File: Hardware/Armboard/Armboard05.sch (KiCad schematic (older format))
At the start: 0 parts

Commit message: Added, Solenoid actuation, laser control, and encoders
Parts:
- added Conn?: Molex_SL_02, symbol MRDT_Connectors:Molex_SL_02
- added D?: LED, symbol Device:LED
- added Q?: Q_NMOS_GSD, symbol Device:Q_NMOS_GSD
- added R?: 1.5k, symbol Device:R
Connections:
- new net: Conn?.2, D?.1 (K), Q?.3 (D)
- new net: D?.2 (A), R?.2
- new net +12V: Conn?.1, R?.1
- new net GND: Q?.2 (S)
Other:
- note added: "Orange"
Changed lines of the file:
@@
 Comment4 ""
 $EndDescr
+$Comp
+L MRDT_Connectors:Molex_SL_02 Conn?
+U 1 1 5F79C943
+P 5850 3250
+F 0 "Conn?" H 5978 3408 60  0000 L CNN
+F 1 "Molex_SL_02" H 5978 3302 60  0000 L CNN
+F 2 "" H 5850 3150 60  0001 C CNN
+F 3 "" H 5850 3150 60  0001 C CNN
+	1    5850 3250
+	1    0    0    -1
+$EndComp
+$Comp
+L power:+12V #PWR?
+U 1 1 5F79C949
+P 5300 2850
+AR Path="/5F73890D/5F79C949" Ref="#PWR?"  Part="1"
+AR Path="/5F738767/5F79C949" Ref="#PWR?"  Part="1"
+F 0 "#PWR?" H 5300 2700 50  0001 C CNN
+F 1 "+12V" H 5315 3023 50  0000 C CNN
+F 2 "" H 5300 2850 50  0001 C CNN
+F 3 "" H 5300 2850 50  0001 C CNN
+	1    5300 2850
+	1    0    0    -1
+$EndComp
+$Comp
+L power:GND #PWR?
+U 1 1 5F79C94F
+P 5300 4850
+F 0 "#PWR?" H 5300 4600 50  0001 C CNN
+F 1 "GND" H 5305 4677 50  0000 C CNN
+F 2 "" H 5300 4850 50  0001 C CNN
+F 3 "" H 5300 4850 50  0001 C CNN
+	1    5300 4850
+	1    0    0    -1
+$EndComp
+$Comp
+L Device:Q_NMOS_GSD Q?
+U 1 1 5F79C957
+P 5200 4400
+F 0 "Q?" H 5404 4446 50  0000 L CNN
+F 1 "Q_NMOS_GSD" H 5404 4355 50  0000 L CNN
+F 2 "" H 5400 4500 50  0001 C CNN
+F 3 "~" H 5200 4400 50  0001 C CNN
+	1    5200 4400
+	1    0    0    -1
+$EndComp
+Wire Wire Line
+	5300 4850 5300 4600
+$Comp
+L Device:R R?
+U 1 1 5F79C95E
+P 5300 3450
+AR Path="/5F73890D/5F79C95E" Ref="R?"  Part="1"
+AR Path="/5F738767/5F79C95E" Ref="R?"  Part="1"
+F 0 "R?" H 5370 3496 50  0000 L CNN
+F 1 "1.5k" H 5370 3405 50  0000 L CNN
+F 2 "" V 5230 3450 50  0001 C CNN
+F 3 "~" H 5300 3450 50  0001 C CNN
+	1    5300 3450
+	1    0    0    -1
+$EndComp
+$Comp
+L Device:LED D?
+U 1 1 5F79C964
+P 5300 3900
+F 0 "D?" V 5339 3782 50  0000 R CNN
+F 1 "LED" V 5248 3782 50  0000 R CNN
+F 2 "" H 5300 3900 50  0001 C CNN
+F 3 "~" H 5300 3900 50  0001 C CNN
+	1    5300 3900
+	0    -1   -1   0
+$EndComp
+Wire Wire Line
+	5300 3750 5300 3600
+Wire Wire Line
+	5300 4200 5300 4150
+Wire Wire Line
+	5650 3200 5600 3200
+Wire Wire Line
+	5650 3100 5300 3100
+Wire Wire Line
+	5300 3100 5300 3300
+Wire Wire Line
+	5600 3200 5600 4150
+Wire Wire Line
+	5600 4150 5300 4150
+Connection ~ 5300 4150
+Wire Wire Line
+	5300 4150 5300 4050
+Wire Wire Line
+	5300 3100 5300 2850
+Connection ~ 5300 3100
+Text Notes 4950 3950 0    50   ~ 0
+Orange
 $EndSCHEMATC

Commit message: H-Bridge completed
Completed the H-Bridge Hierarchal Sheet
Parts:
- Conn?: symbol MRDT_Connectors:Molex_SL_02 -> Armboard-rescue:Molex_SL_02-MRDT_Connectors
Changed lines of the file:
@@
 $EndDescr
 $Comp
-L MRDT_Connectors:Molex_SL_02 Conn?
+L Armboard-rescue:Molex_SL_02-MRDT_Connectors Conn?
 U 1 1 5F79C943
 P 5850 3250

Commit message: Added serial pins, limit switches, titles, and indicators
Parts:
- added D?: LED, symbol Device:LED
- added R?: 500, symbol Device:R
- Conn?: symbol Armboard-rescue:Molex_SL_02-MRDT_Connectors -> Armboard-rescue:Molex_SL_02-MRDT_Connectors-Armboard-rescue
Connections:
- net GND: now also D?.1 (K)
- net Solenoid_Actuation: now reaches Q?.1 (G)
- net Solenoid_Actuation: now also R?.1
- new net: D?.2 (A), R?.2
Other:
- note added: "Solenoid Actuation"
- note added: "Yellow"
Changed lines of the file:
@@
 $EndDescr
 $Comp
-L Armboard-rescue:Molex_SL_02-MRDT_Connectors Conn?
+L Armboard-rescue:Molex_SL_02-MRDT_Connectors-Armboard-rescue Conn?
 U 1 1 5F79C943
 P 5850 3250
@@
 Text Notes 4950 3950 0    50   ~ 0
 Orange
+Text GLabel 4500 4400 0    50   Input ~ 0
+Solenoid_Actuation
+$Comp
+L Device:R R?
+U 1 1 5F8410BE
+P 4750 4700
+AR Path="/5F73890D/5F8410BE" Ref="R?"  Part="1"
+AR Path="/5F738767/5F8410BE" Ref="R?"  Part="1"
+F 0 "R?" H 4820 4746 50  0000 L CNN
+F 1 "500" H 4820 4655 50  0000 L CNN
+F 2 "" V 4680 4700 50  0001 C CNN
+F 3 "~" H 4750 4700 50  0001 C CNN
+	1    4750 4700
+	1    0    0    -1
+$EndComp
+$Comp
+L Device:LED D?
+U 1 1 5F841F2B
+P 4750 5100
+F 0 "D?" V 4789 4982 50  0000 R CNN
+F 1 "LED" V 4698 4982 50  0000 R CNN
+F 2 "" H 4750 5100 50  0001 C CNN
+F 3 "~" H 4750 5100 50  0001 C CNN
+	1    4750 5100
+	0    -1   -1   0
+$EndComp
+Text Notes 4400 5150 0    50   ~ 0
+Yellow
+$Comp
+L power:GND #PWR?
+U 1 1 5F842098
+P 4750 5350
+F 0 "#PWR?" H 4750 5100 50  0001 C CNN
+F 1 "GND" H 4755 5177 50  0000 C CNN
+F 2 "" H 4750 5350 50  0001 C CNN
+F 3 "" H 4750 5350 50  0001 C CNN
+	1    4750 5350
+	1    0    0    -1
+$EndComp
+Wire Wire Line
+	4500 4400 4750 4400
+Wire Wire Line
+	4750 4550 4750 4400
+Connection ~ 4750 4400
+Wire Wire Line
+	4750 4400 5000 4400
+Wire Wire Line
+	4750 4950 4750 4850
+Wire Wire Line
+	4750 5350 4750 5250
+Text Notes 6500 7150 0    157  ~ 31
+Solenoid Actuation
 $EndSCHEMATC

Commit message: Tiva Updates
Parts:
- added SW?: SW_Push, symbol Switch:SW_Push
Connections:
- net +12V: now also SW?.2; no longer R?.1
- new net: R?.1, SW?.1
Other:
- moved on the sheet: Conn?
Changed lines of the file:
@@
 L Armboard-rescue:Molex_SL_02-MRDT_Connectors-Armboard-rescue Conn?
 U 1 1 5F79C943
-P 5850 3250
-F 0 "Conn?" H 5978 3408 60  0000 L CNN
-F 1 "Molex_SL_02" H 5978 3302 60  0000 L CNN
-F 2 "" H 5850 3150 60  0001 C CNN
-F 3 "" H 5850 3150 60  0001 C CNN
-	1    5850 3250
+P 5850 2750
+F 0 "Conn?" H 5978 2908 60  0000 L CNN
+F 1 "Molex_SL_02" H 5978 2802 60  0000 L CNN
+F 2 "" H 5850 2650 60  0001 C CNN
+F 3 "" H 5850 2650 60  0001 C CNN
+	1    5850 2750
 	1    0    0    -1
 $EndComp
@@
 L power:+12V #PWR?
 U 1 1 5F79C949
-P 5300 2850
+P 5300 2350
 AR Path="/5F73890D/5F79C949" Ref="#PWR?"  Part="1"
 AR Path="/5F738767/5F79C949" Ref="#PWR?"  Part="1"
-F 0 "#PWR?" H 5300 2700 50  0001 C CNN
-F 1 "+12V" H 5315 3023 50  0000 C CNN
-F 2 "" H 5300 2850 50  0001 C CNN
-F 3 "" H 5300 2850 50  0001 C CNN
-	1    5300 2850
+F 0 "#PWR?" H 5300 2200 50  0001 C CNN
+F 1 "+12V" H 5315 2523 50  0000 C CNN
+F 2 "" H 5300 2350 50  0001 C CNN
+F 3 "" H 5300 2350 50  0001 C CNN
+	1    5300 2350
 	1    0    0    -1
 $EndComp
@@
 	5300 4200 5300 4150
 Wire Wire Line
-	5650 3200 5600 3200
+	5650 2700 5600 2700
 Wire Wire Line
-	5650 3100 5300 3100
+	5650 2600 5300 2600
 Wire Wire Line
-	5300 3100 5300 3300
-Wire Wire Line
-	5600 3200 5600 4150
+	5300 2600 5300 2800
 Wire Wire Line
 	5600 4150 5300 4150
@@
 	5300 4150 5300 4050
 Wire Wire Line
-	5300 3100 5300 2850
-Connection ~ 5300 3100
+	5300 2600 5300 2350
+Connection ~ 5300 2600
 Text Notes 4950 3950 0    50   ~ 0
 Orange
@@
 Text Notes 6500 7150 0    157  ~ 31
 Solenoid Actuation
+$Comp
+L Switch:SW_Push SW?
+U 1 1 5F84F95E
+P 5300 3000
+F 0 "SW?" V 5340 3280 50  0000 R CNN
+F 1 "SW_Push" V 5260 3460 50  0000 R CNN
+F 2 "" H 5300 3200 50  0001 C CNN
+F 3 "~" H 5300 3200 50  0001 C CNN
+	1    5300 3000
+	0    -1   -1   0
+$EndComp
+Wire Wire Line
+	5300 3200 5300 3300
+Wire Wire Line
+	5600 2700 5600 4150
 $EndSCHEMATC

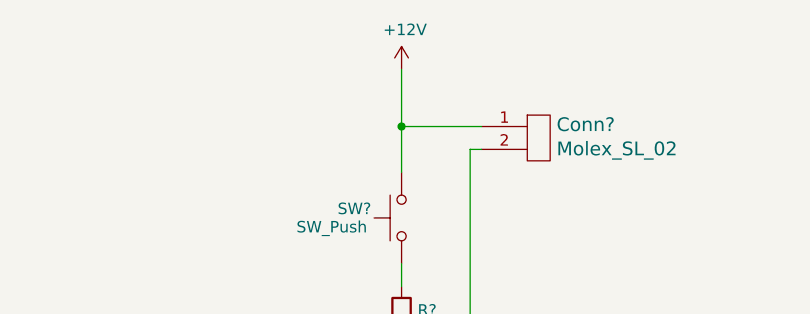
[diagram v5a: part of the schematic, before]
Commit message: Fixed changes from review 2 of circuit board
except the LED indicators
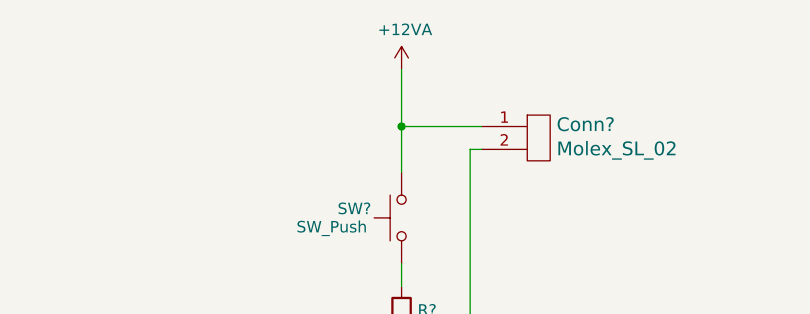
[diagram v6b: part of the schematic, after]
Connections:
- net +12V renamed +12VA
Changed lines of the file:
@@
-$EndComp
-$Comp
-L power:+12V #PWR?
-U 1 1 5F79C949
-P 5300 2350
-AR Path="/5F73890D/5F79C949" Ref="#PWR?"  Part="1"
-AR Path="/5F738767/5F79C949" Ref="#PWR?"  Part="1"
-F 0 "#PWR?" H 5300 2200 50  0001 C CNN
-F 1 "+12V" H 5315 2523 50  0000 C CNN
-F 2 "" H 5300 2350 50  0001 C CNN
-F 3 "" H 5300 2350 50  0001 C CNN
-	1    5300 2350
-	1    0    0    -1
 $EndComp
 $Comp
@@
 Wire Wire Line
 	5600 2700 5600 4150
+$Comp
+L power:+12VA #PWR?
+U 1 1 5F9AC0A0
+P 5300 2350
+F 0 "#PWR?" H 5300 2200 50  0001 C CNN
+F 1 "+12VA" H 5315 2523 50  0000 C CNN
+F 2 "" H 5300 2350 50  0001 C CNN
+F 3 "" H 5300 2350 50  0001 C CNN
+	1    5300 2350
+	1    0    0    -1
+$EndComp
 $EndSCHEMATC
